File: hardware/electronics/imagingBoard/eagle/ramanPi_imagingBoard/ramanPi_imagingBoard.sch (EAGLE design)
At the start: 16 parts

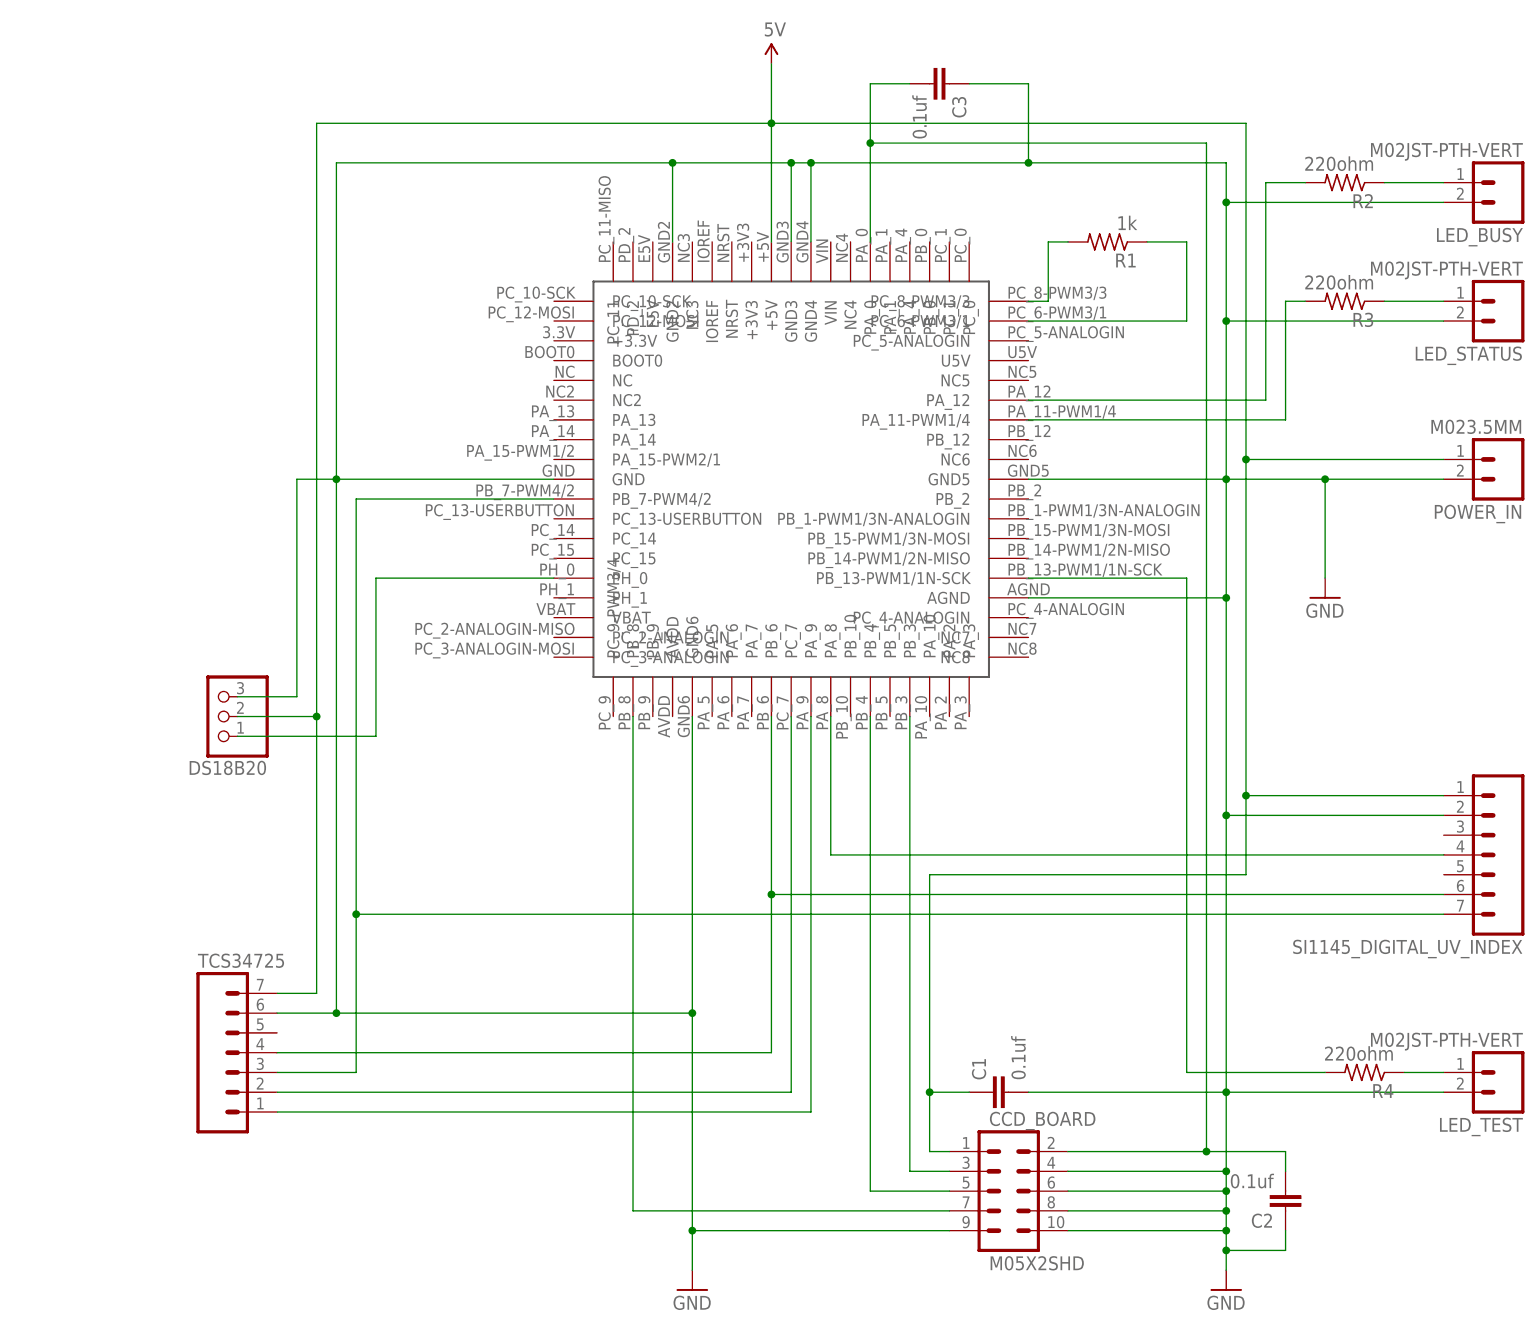
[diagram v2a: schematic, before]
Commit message: added reset circuitry to all stm32 boards
added reset circuitry for raspi to reset each board from remote.
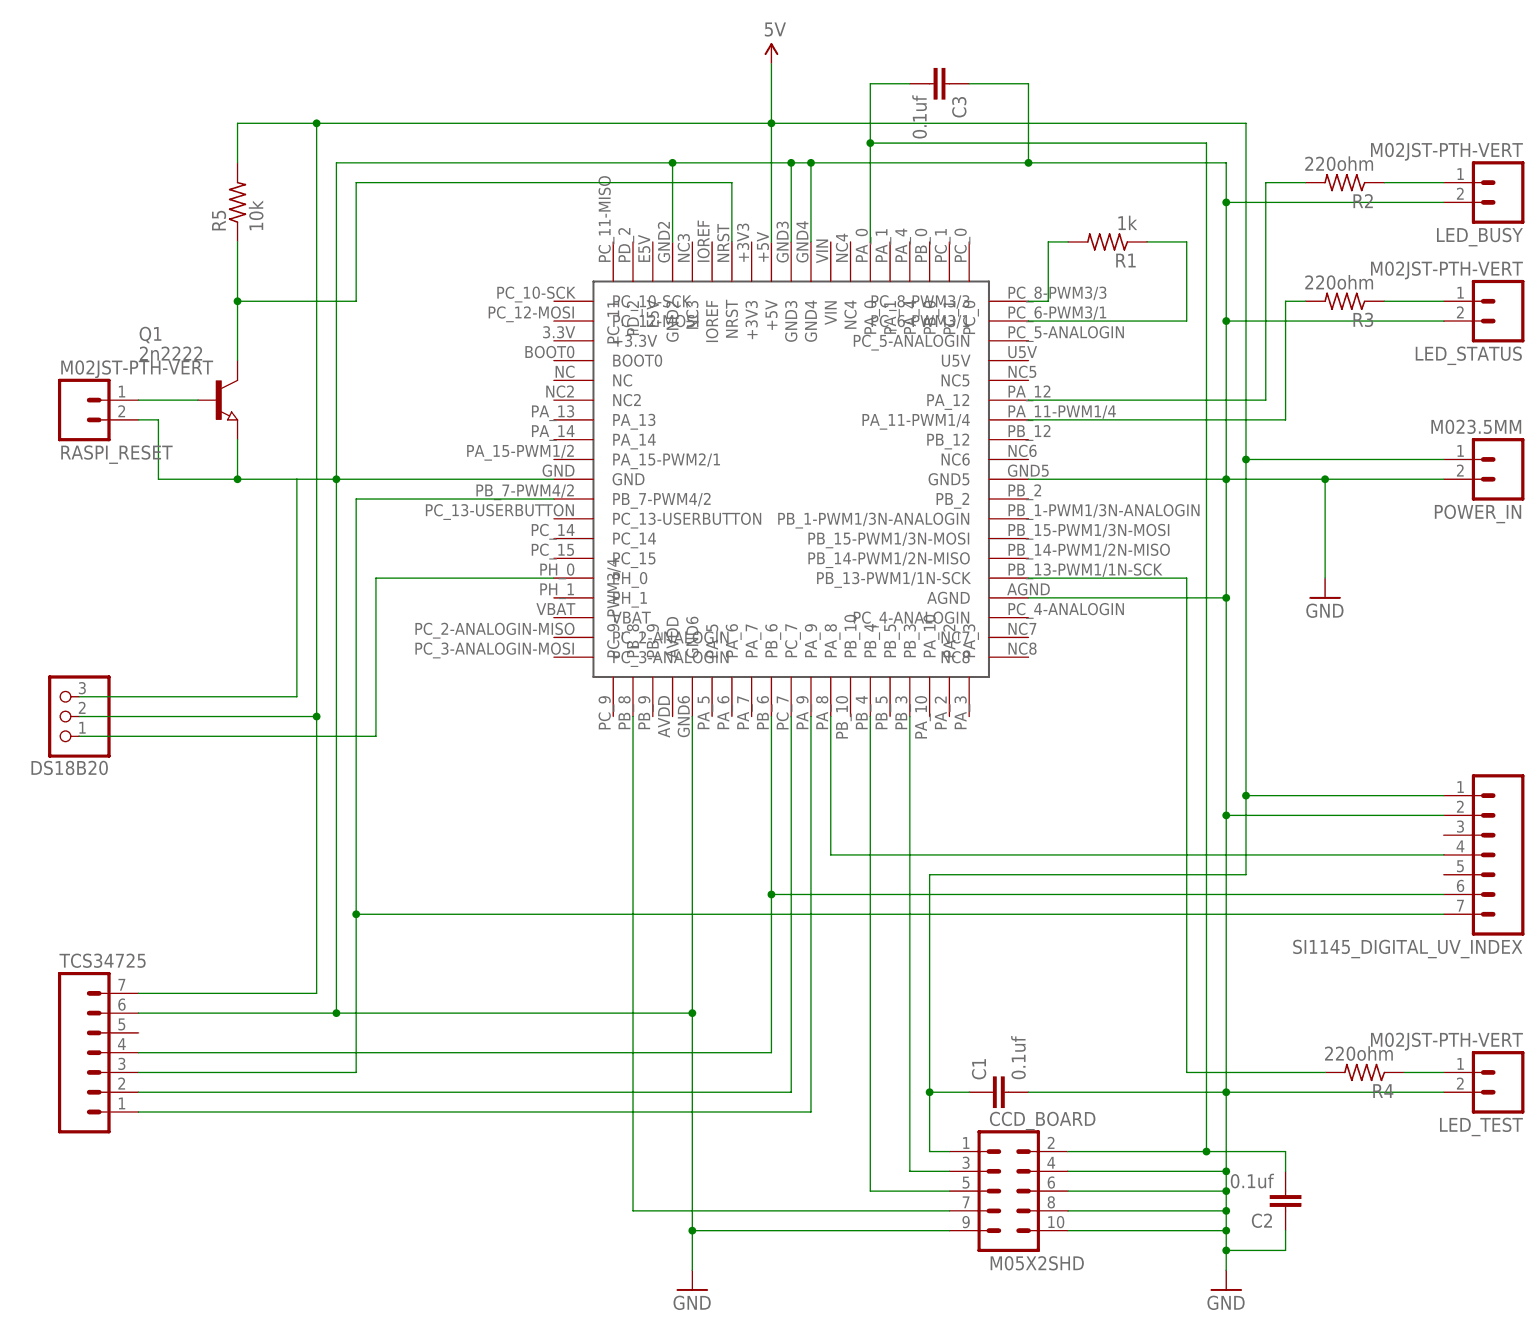
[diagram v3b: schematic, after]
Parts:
- added Q1: 2n2222, semicon-smd-ipc:NPN-TRANSISTOR_SOT23
- added R5: 10k, adafruit:R-US_M1206
- added RASPI_RESET: M02JST-PTH-VERT, SparkFun-Connectors:M02JST-PTH-VERT
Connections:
- new net N$19: Q1.C, R5.1, U$1.NRST
- new net N$3: Q1.B, RASPI_RESET.1
- net 5V: now also R5.2
- net GND: now also Q1.E, RASPI_RESET.2
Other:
- moved on the sheet: DS18B20, TCS34725
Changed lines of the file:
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@@
 <part name="C2" library="SparkFun-Capacitors" deviceset="CAP" device="1210" value="0.1uf"/>
 <part name="C3" library="SparkFun-Capacitors" deviceset="CAP" device="1210" value="0.1uf"/>
+<part name="Q1" library="semicon-smd-ipc" deviceset="NPN-TRANSISTOR_" device="SOT23" value="2n2222"/>
+<part name="R5" library="adafruit" deviceset="R-US_" device="M1206" value="10k"/>
+<part name="RASPI_RESET" library="SparkFun-Connectors" deviceset="M02" device="JST-PTH-VERT"/>
 </parts>
 <sheets>
@@
 <instance part="GND2" gate="1" x="165.1" y="96.52"/>
 <instance part="R1" gate="G$1" x="137.16" y="142.24" rot="R180"/>
-<instance part="DS18B20" gate="A" x="22.86" y="81.28" rot="R180"/>
+<instance part="DS18B20" gate="A" x="2.54" y="81.28" rot="R180"/>
 <instance part="CCD_BOARD" gate="G$1" x="124.46" y="20.32"/>
 <instance part="GND3" gate="1" x="152.4" y="7.62"/>
-<instance part="TCS34725" gate="G$1" x="25.4" y="35.56"/>
+<instance part="TCS34725" gate="G$1" x="7.62" y="35.56"/>
 <instance part="POWER_IN" gate="G$1" x="187.96" y="114.3" rot="R180"/>
 <instance part="LED_STATUS" gate="G$1" x="187.96" y="134.62" rot="R180"/>
@@
 <instance part="C2" gate="G$1" x="160.02" y="20.32" rot="R180"/>
 <instance part="C3" gate="G$1" x="114.3" y="162.56" rot="R270"/>
+<instance part="Q1" gate="G$1" x="22.86" y="121.92"/>
+<instance part="R5" gate="G$1" x="25.4" y="147.32" rot="R90"/>
+<instance part="RASPI_RESET" gate="G$1" x="5.08" y="121.92" rot="MR180"/>
 </instances>
 <busses>
@@
 <wire x1="40.64" y1="55.88" x2="180.34" y2="55.88" width="0.1524" layer="91"/>
 <pinref part="TCS34725" gate="G$1" pin="3"/>
-<wire x1="30.48" y1="35.56" x2="40.64" y2="35.56" width="0.1524" layer="91"/>
+<wire x1="12.7" y1="35.56" x2="40.64" y2="35.56" width="0.1524" layer="91"/>
 <wire x1="40.64" y1="35.56" x2="40.64" y2="55.88" width="0.1524" layer="91"/>
 <junction x="40.64" y="55.88"/>
@@
 <wire x1="93.98" y1="58.42" x2="180.34" y2="58.42" width="0.1524" layer="91"/>
 <pinref part="TCS34725" gate="G$1" pin="4"/>
-<wire x1="30.48" y1="38.1" x2="93.98" y2="38.1" width="0.1524" layer="91"/>
+<wire x1="12.7" y1="38.1" x2="93.98" y2="38.1" width="0.1524" layer="91"/>
 <wire x1="93.98" y1="38.1" x2="93.98" y2="58.42" width="0.1524" layer="91"/>
 <junction x="93.98" y="58.42"/>
@@
 <wire x1="152.4" y1="111.76" x2="165.1" y2="111.76" width="0.1524" layer="91"/>
 <wire x1="165.1" y1="111.76" x2="165.1" y2="99.06" width="0.1524" layer="91"/>
-<wire x1="25.4" y1="83.82" x2="33.02" y2="83.82" width="0.1524" layer="91"/>
+<wire x1="5.08" y1="83.82" x2="33.02" y2="83.82" width="0.1524" layer="91"/>
 <wire x1="33.02" y1="83.82" x2="33.02" y2="111.76" width="0.1524" layer="91"/>
 <wire x1="33.02" y1="111.76" x2="38.1" y2="111.76" width="0.1524" layer="91"/>
@@
 <pinref part="GND1" gate="1" pin="GND"/>
 <pinref part="TCS34725" gate="G$1" pin="6"/>
-<wire x1="30.48" y1="43.18" x2="38.1" y2="43.18" width="0.1524" layer="91"/>
+<wire x1="12.7" y1="43.18" x2="38.1" y2="43.18" width="0.1524" layer="91"/>
 <wire x1="38.1" y1="43.18" x2="83.82" y2="43.18" width="0.1524" layer="91"/>
 <wire x1="83.82" y1="43.18" x2="83.82" y2="15.24" width="0.1524" layer="91"/>
@@
 <wire x1="127" y1="162.56" x2="127" y2="152.4" width="0.1524" layer="91"/>
 <junction x="127" y="152.4"/>
+<pinref part="Q1" gate="G$1" pin="E"/>
+<wire x1="25.4" y1="116.84" x2="25.4" y2="111.76" width="0.1524" layer="91"/>
+<wire x1="25.4" y1="111.76" x2="33.02" y2="111.76" width="0.1524" layer="91"/>
+<pinref part="RASPI_RESET" gate="G$1" pin="2"/>
+<wire x1="12.7" y1="119.38" x2="15.24" y2="119.38" width="0.1524" layer="91"/>
+<wire x1="15.24" y1="119.38" x2="15.24" y2="111.76" width="0.1524" layer="91"/>
+<wire x1="15.24" y1="111.76" x2="25.4" y2="111.76" width="0.1524" layer="91"/>
+<junction x="25.4" y="111.76"/>
 </segment>
 </net>
@@
 <pinref part="SUPPLY1" gate="G$1" pin="5V"/>
 <wire x1="93.98" y1="157.48" x2="93.98" y2="165.1" width="0.1524" layer="91"/>
-<wire x1="25.4" y1="81.28" x2="35.56" y2="81.28" width="0.1524" layer="91"/>
+<wire x1="5.08" y1="81.28" x2="35.56" y2="81.28" width="0.1524" layer="91"/>
 <pinref part="DS18B20" gate="A" pin="2"/>
 <wire x1="154.94" y1="71.12" x2="154.94" y2="60.96" width="0.1524" layer="91"/>
@@
 <wire x1="35.56" y1="81.28" x2="35.56" y2="45.72" width="0.1524" layer="91"/>
 <pinref part="TCS34725" gate="G$1" pin="7"/>
-<wire x1="35.56" y1="45.72" x2="30.48" y2="45.72" width="0.1524" layer="91"/>
+<wire x1="35.56" y1="45.72" x2="12.7" y2="45.72" width="0.1524" layer="91"/>
 <junction x="35.56" y="81.28"/>
 <pinref part="POWER_IN" gate="G$1" pin="1"/>
@@
 <wire x1="114.3" y1="33.02" x2="119.38" y2="33.02" width="0.1524" layer="91"/>
 <junction x="114.3" y="33.02"/>
+<pinref part="R5" gate="G$1" pin="2"/>
+<wire x1="25.4" y1="152.4" x2="25.4" y2="157.48" width="0.1524" layer="91"/>
+<wire x1="25.4" y1="157.48" x2="35.56" y2="157.48" width="0.1524" layer="91"/>
+<junction x="35.56" y="157.48"/>
 </segment>
 </net>
@@
 <wire x1="43.18" y1="99.06" x2="66.04" y2="99.06" width="0.1524" layer="91"/>
 <wire x1="43.18" y1="99.06" x2="43.18" y2="78.74" width="0.1524" layer="91"/>
-<wire x1="43.18" y1="78.74" x2="25.4" y2="78.74" width="0.1524" layer="91"/>
+<wire x1="43.18" y1="78.74" x2="5.08" y2="78.74" width="0.1524" layer="91"/>
 <pinref part="DS18B20" gate="A" pin="1"/>
 </segment>
@@
 <pinref part="TCS34725" gate="G$1" pin="2"/>
 <pinref part="U$1" gate="G$1" pin="PC_7"/>
-<wire x1="30.48" y1="33.02" x2="96.52" y2="33.02" width="0.1524" layer="91"/>
+<wire x1="12.7" y1="33.02" x2="96.52" y2="33.02" width="0.1524" layer="91"/>
 <wire x1="96.52" y1="33.02" x2="96.52" y2="81.28" width="0.1524" layer="91"/>
 </segment>
@@
 <segment>
 <pinref part="TCS34725" gate="G$1" pin="1"/>
-<wire x1="30.48" y1="30.48" x2="99.06" y2="30.48" width="0.1524" layer="91"/>
+<wire x1="12.7" y1="30.48" x2="99.06" y2="30.48" width="0.1524" layer="91"/>
 <pinref part="U$1" gate="G$1" pin="PA_9"/>
 <wire x1="99.06" y1="30.48" x2="99.06" y2="81.28" width="0.1524" layer="91"/>
@@
 </segment>
 </net>
+<net name="N$19" class="0">
+<segment>
+<pinref part="U$1" gate="G$1" pin="NRST"/>
+<wire x1="88.9" y1="142.24" x2="88.9" y2="149.86" width="0.1524" layer="91"/>
+<wire x1="88.9" y1="149.86" x2="40.64" y2="149.86" width="0.1524" layer="91"/>
+<wire x1="40.64" y1="149.86" x2="40.64" y2="134.62" width="0.1524" layer="91"/>
+<wire x1="40.64" y1="134.62" x2="25.4" y2="134.62" width="0.1524" layer="91"/>
+<pinref part="Q1" gate="G$1" pin="C"/>
+<wire x1="25.4" y1="134.62" x2="25.4" y2="127" width="0.1524" layer="91"/>
+<pinref part="R5" gate="G$1" pin="1"/>
+<wire x1="25.4" y1="134.62" x2="25.4" y2="142.24" width="0.1524" layer="91"/>
+<junction x="25.4" y="134.62"/>
+</segment>
+</net>
+<net name="N$3" class="0">
+<segment>
+<pinref part="RASPI_RESET" gate="G$1" pin="1"/>
+<pinref part="Q1" gate="G$1" pin="B"/>
+<wire x1="12.7" y1="121.92" x2="20.32" y2="121.92" width="0.1524" layer="91"/>
+</segment>
+</net>
